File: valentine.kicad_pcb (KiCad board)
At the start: 2 copper layers, 20 x 32.2 mm, 0 parts

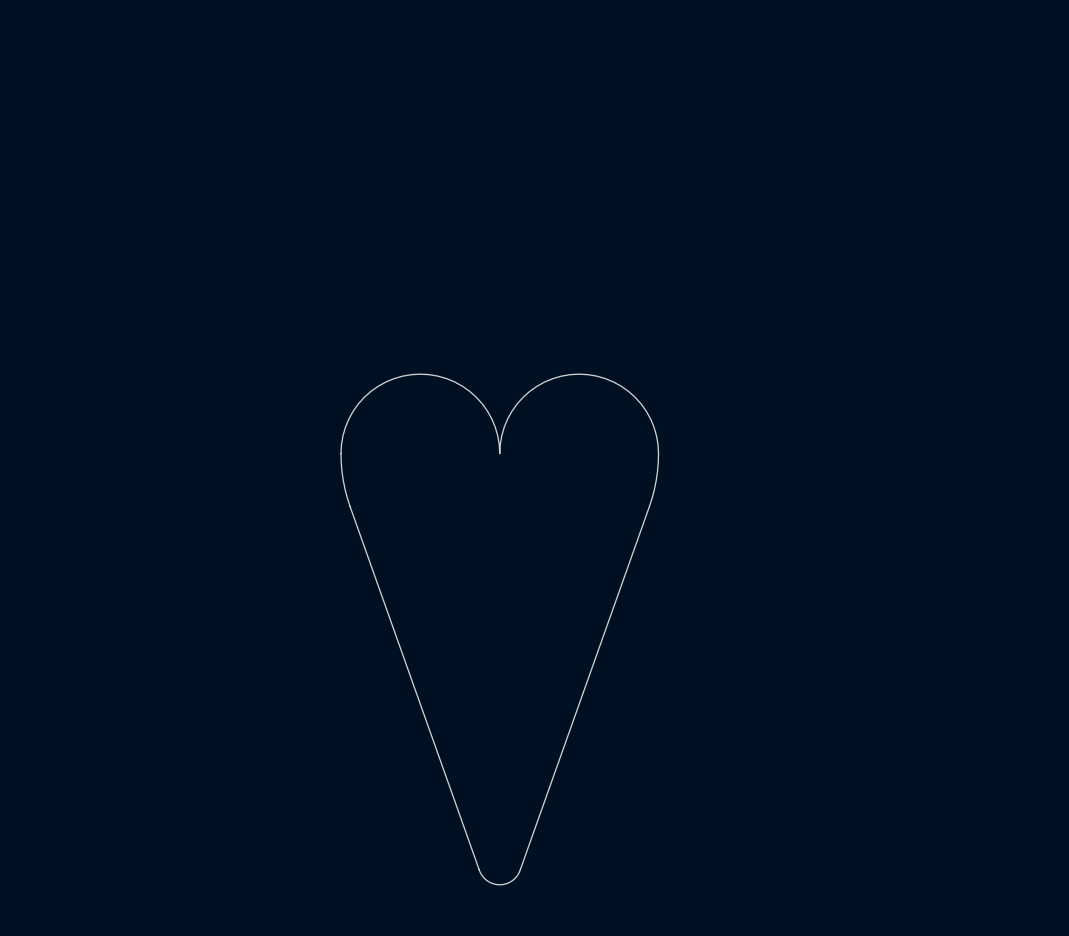
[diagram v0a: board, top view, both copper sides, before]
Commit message: pcb design done ,,design as in where to put what i made a grid
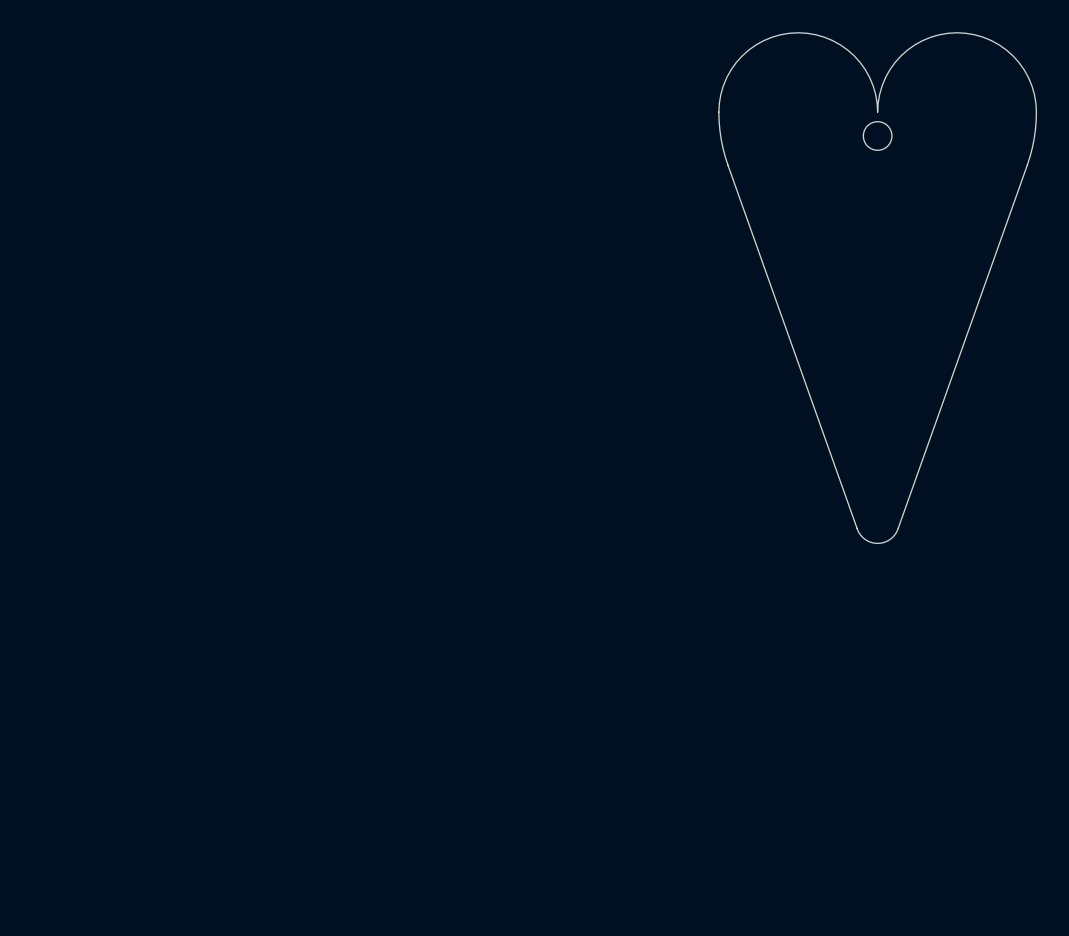
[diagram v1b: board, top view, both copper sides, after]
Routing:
- added copper zone on In2.Cu, net +3.3V
- added copper zone on In1.Cu, net GND
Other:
- outline, holes or cut-outs redrawn
- copper layers 2 -> 4

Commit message: pcb routing
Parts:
- added C1: 100nF, Capacitor_SMD:C_0603_1608Metric, F.Cu at (167.8, 105.9)
- added C2: 4.7uF, Capacitor_SMD:C_0805_2012Metric, F.Cu at (175.3, 111.2)
- added C3: 100nF, Capacitor_SMD:C_0603_1608Metric, F.Cu at (167.8, 108.4)
- added C4: 10uF, Capacitor_SMD:C_0805_2012Metric, F.Cu at (175.3, 114.2)
- added D1: LED, LED_SMD:LED_0603_1608Metric, F.Cu at (212.8, 62.5)
- added D10: LED, LED_SMD:LED_0603_1608Metric, F.Cu at (221.3, 85.2)
- added D11: LED, LED_SMD:LED_0603_1608Metric, F.Cu at (223.0, 80.2)
- added D12: LED, LED_SMD:LED_0603_1608Metric, F.Cu at (224.8, 75.2)
- added D13: LED, LED_SMD:LED_0603_1608Metric, F.Cu at (226.4, 70.8)
- added D14: LED, LED_SMD:LED_0603_1608Metric, F.Cu at (227.6, 67.5)
- added D15: LED, LED_SMD:LED_0603_1608Metric, F.Cu at (222.0, 83.4)
- added D16: LED, LED_SMD:LED_0603_1608Metric, F.Cu at (226.8, 62.4)
- added D2: LED, LED_SMD:LED_0603_1608Metric, F.Cu at (212.0, 67.5)
- added D3: LED, LED_SMD:LED_0603_1608Metric, F.Cu at (213.2, 70.8)
- added D4: LED, LED_SMD:LED_0603_1608Metric, F.Cu at (214.8, 75.2)
- added D5: LED, LED_SMD:LED_0603_1608Metric, F.Cu at (216.5, 80.2)
- added D6: LED, LED_SMD:LED_0603_1608Metric, F.Cu at (217.8, 83.5)
- added D7: LED, LED_SMD:LED_0603_1608Metric, F.Cu at (218.2, 85.2)
- added D8: LED, LED_SMD:LED_0603_1608Metric, F.Cu at (219.0, 89.0)
- added D9: LED, LED_SMD:LED_0603_1608Metric, F.Cu at (220.6, 89.0)
- added J1: Conn_01x04_Socket, Connector_PinSocket_1.27mm:PinSocket_2x02_P1.27mm_Vertical_SMD, B.Cu at (219.8, 80.6)
- added J2: Battery, Connector_PinHeader_1.00mm:PinHeader_1x02_P1.00mm_Vertical_SMD_Pin1Right, F.Cu at (182.4, 113.5)
- added R10: 1.8K, Resistor_SMD:R_0402_1005Metric, F.Cu at (223.3, 81.8)
- added R11: 1.8K, Resistor_SMD:R_0402_1005Metric, F.Cu at (225.1, 76.8)
- added R12: 1.8K, Resistor_SMD:R_0402_1005Metric, F.Cu at (226.7, 72.2)
- added R13: 1.8K, Resistor_SMD:R_0402_1005Metric, F.Cu at (227.8, 69.0)
- added R14: 1.8K, Resistor_SMD:R_0402_1005Metric, B.Cu at (222.0, 83.4)
- added R15: 1.8K, Resistor_SMD:R_0402_1005Metric, F.Cu at (227.6, 64.0)
- added R17: 1.8K, Resistor_SMD:R_0402_1005Metric, B.Cu at (218.2, 85.2)
- added R18: 1.8K, Resistor_SMD:R_0402_1005Metric, B.Cu at (219.0, 89.0)
- added R2: 1.8K, Resistor_SMD:R_0402_1005Metric, F.Cu at (214.5, 76.8)
- added R3: 1.8K, Resistor_SMD:R_0402_1005Metric, F.Cu at (216.2, 81.8)
- added R4: 1.8K, Resistor_SMD:R_0402_1005Metric, B.Cu at (217.6, 83.5)
- added R5: 1.8K, Resistor_SMD:R_0402_1005Metric, F.Cu at (212.0, 64.0)
- added R6: 1.8K, Resistor_SMD:R_0402_1005Metric, F.Cu at (211.8, 69.0)
- added R7: 1.8K, Resistor_SMD:R_0402_1005Metric, F.Cu at (213.0, 72.2)
- added R8: 1.8K, Resistor_SMD:R_0402_1005Metric, B.Cu at (220.6, 89.0)
- added R9: 1.8K, Resistor_SMD:R_0402_1005Metric, B.Cu at (221.4, 85.2)
- added SW1: SW_Push_45deg, Button_Switch_SMD:SW_Push_SPST_NO_Alps_SKRK, F.Cu at (176.4, 107.4)
- added U1: STM32G031G8Ux, Package_DFN_QFN:QFN-28_4x4mm_P0.5mm, F.Cu at (219.8, 76.1)
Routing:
- net GND: track 0.00 -> 23.3 mm, vias 0 -> 13
- net /PB0: track 0.00 -> 15.1 mm, vias 0 -> 3
- net /PB8: track 0.00 -> 13.9 mm
- net /PA0: track 0.00 -> 13.8 mm
- net /PA6: track 0.00 -> 13.5 mm, vias 0 -> 2
- net /PA7: track 0.00 -> 13.1 mm, vias 0 -> 2
- net /PB7: track 0.00 -> 11.0 mm, vias 0 -> 2
- net /PB6: track 0.00 -> 10.6 mm
- net /PA5: track 0.00 -> 9.79 mm, vias 0 -> 2
- net /PB1: track 0.00 -> 9.21 mm, vias 0 -> 2
- net /PA4: track 0.00 -> 9.05 mm, vias 0 -> 2
- net /PA1: track 0.00 -> 9.02 mm
- net /NRST: track 0.00 -> 8.82 mm, vias 0 -> 2
- net /PB5: track 0.00 -> 7.40 mm
- net /PA2: track 0.00 -> 5.41 mm
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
